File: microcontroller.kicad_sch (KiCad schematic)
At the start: 23 parts, among them J11 VOX_IN, J12 VOX_TRX, J6 I2C, J7 SW1_CON, J8 I2C, SW1 SW_Push, U3 ESP32-DEVKIT

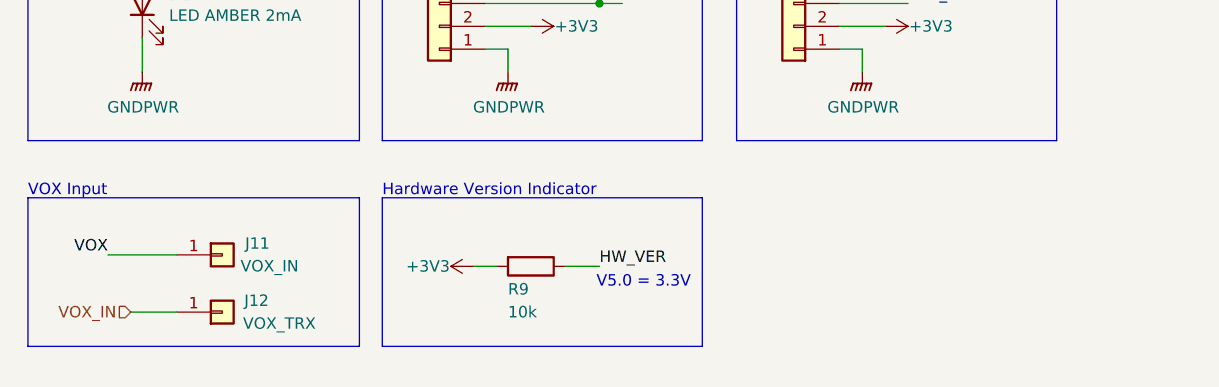
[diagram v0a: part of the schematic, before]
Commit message: am: Modified HW indication voltage
* Added R10 for voltage divider (v6.x == 1.65V)
* Replaced all R footprints with current ones from KiCad lib
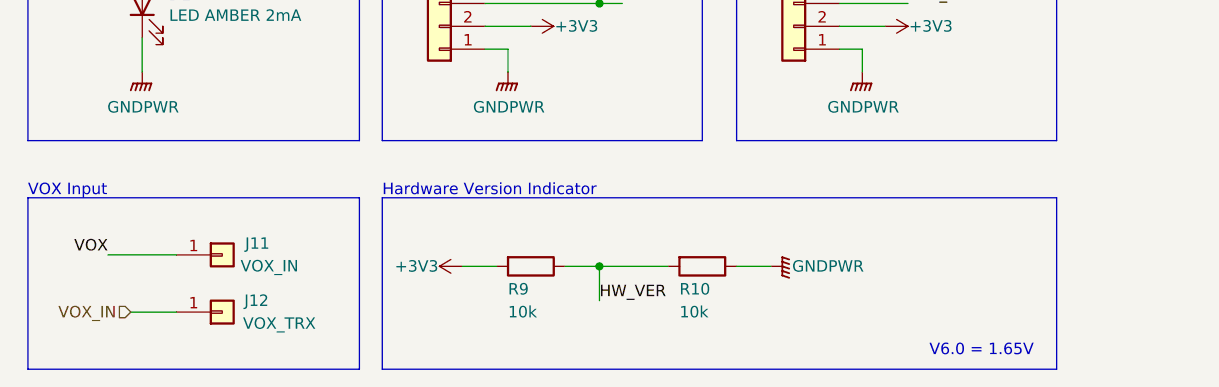
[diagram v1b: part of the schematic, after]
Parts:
- added R10: 10k, Resistor_SMD:R_0805_2012Metric_Pad1.20x1.40mm_HandSolder, symbol Device:R
- R2, R3, R4, R5, R6, R7, R9: footprint Resistor_SMD:R_0805_2012Metric_Pad1.15x1.40mm_HandSolder -> Resistor_SMD:R_0805_2012Metric_Pad1.20x1.40mm_HandSolder
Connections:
- net GNDPWR: now also R10.1
- net HW_VER: now also R10.2
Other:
- note added: "V6.0 = 1.65V"
- note removed: "V5.0 = 3.3V"
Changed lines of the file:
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@@
   (junction (at 30.48 72.39) (diameter 0) (color 0 0 0 0)
+  )
+  (junction (at 81.28 152.4) (diameter 0) (color 0 0 0 0)
   )
   (junction (at 24.13 72.39) (diameter 0) (color 0 0 0 0)
@@
     (stroke (width 0) (type default) (color 0 0 0 0))
   )
-  (polyline (pts (xy 54.61 144.78) (xy 54.61 161.29))
+  (polyline (pts (xy 54.61 144.78) (xy 54.61 163.83))
     (stroke (width 0) (type default) (color 0 0 0 0))
   )
@@
     (stroke (width 0) (type default) (color 0 0 0 0))
   )
-  (polyline (pts (xy 57.15 161.29) (xy 92.71 161.29))
+  (polyline (pts (xy 57.15 163.83) (xy 132.08 163.83))
     (stroke (width 0) (type default) (color 0 0 0 0))
   )
@@
     (stroke (width 0) (type default) (color 0 0 0 0))
   )
-  (polyline (pts (xy 92.71 144.78) (xy 57.15 144.78))
+  (polyline (pts (xy 132.08 144.78) (xy 57.15 144.78))
     (stroke (width 0) (type default) (color 0 0 0 0))
   )
@@
     (stroke (width 0) (type default) (color 0 0 0 0))
   )
-  (polyline (pts (xy 57.15 144.78) (xy 57.15 161.29))
+  (polyline (pts (xy 57.15 144.78) (xy 57.15 163.83))
     (stroke (width 0) (type default) (color 0 0 0 0))
   )
@@
     (stroke (width 0) (type default) (color 0 0 0 0))
   )
-  (wire (pts (xy 67.31 152.4) (xy 69.85 152.4))
-    (stroke (width 0) (type default) (color 0 0 0 0))
-  )
   (wire (pts (xy 81.28 116.84) (xy 81.28 123.19))
     (stroke (width 0) (type default) (color 0 0 0 0))
@@
     (stroke (width 0) (type default) (color 0 0 0 0))
   )
-  (polyline (pts (xy 17.78 144.78) (xy 17.78 161.29))
+  (polyline (pts (xy 17.78 144.78) (xy 17.78 163.83))
     (stroke (width 0) (type default) (color 0 0 0 0))
   )
@@
     (stroke (width 0) (type default) (color 0 0 0 0))
   )
-  (polyline (pts (xy 92.71 144.78) (xy 92.71 161.29))
+  (polyline (pts (xy 132.08 144.78) (xy 132.08 163.83))
     (stroke (width 0) (type default) (color 0 0 0 0))
   )
@@
     (stroke (width 0) (type default) (color 0 0 0 0))
   )
+  (wire (pts (xy 81.28 152.4) (xy 81.28 156.21))
+    (stroke (width 0) (type default) (color 0 0 0 0))
+  )
   (wire (pts (xy 171.45 58.42) (xy 175.26 58.42))
     (stroke (width 0) (type default) (color 0 0 0 0))
@@
     (stroke (width 0) (type default) (color 0 0 0 0))
   )
-  (polyline (pts (xy 54.61 161.29) (xy 17.78 161.29))
+  (polyline (pts (xy 54.61 163.83) (xy 17.78 163.83))
     (stroke (width 0) (type default) (color 0 0 0 0))
   )
@@
     (stroke (width 0) (type default) (color 0 0 0 0))
   )
+  (wire (pts (xy 96.52 152.4) (xy 100.33 152.4))
+    (stroke (width 0) (type default) (color 0 0 0 0))
+  )
   (wire (pts (xy 25.4 26.67) (xy 31.75 26.67))
     (stroke (width 0) (type default) (color 0 0 0 0))
@@
     (stroke (width 0) (type default) (color 0 0 0 0))
   )
+  (wire (pts (xy 81.28 152.4) (xy 88.9 152.4))
+    (stroke (width 0) (type default) (color 0 0 0 0))
+  )
   (wire (pts (xy 62.23 69.85) (xy 62.23 73.66))
     (stroke (width 0) (type default) (color 0 0 0 0))
   )
   (polyline (pts (xy 17.78 97.79) (xy 17.78 138.43))
+    (stroke (width 0) (type default) (color 0 0 0 0))
+  )
+  (wire (pts (xy 66.04 152.4) (xy 69.85 152.4))
     (stroke (width 0) (type default) (color 0 0 0 0))
   )
@@
     (effects (font (size 1.27 1.27)) (justify left bottom))
   )
-  (text "V5.0 = 3.3V" (at 91.44 154.94 180)
+  (text "V6.0 = 1.65V" (at 129.54 162.56 180)
     (effects (font (size 1.27 1.27)) (justify right bottom))
   )
@@
     (effects (font (size 1.27 1.27)) (justify right bottom))
   )
-  (label "HW_VER" (at 81.28 152.4 0)
+  (label "HW_VER" (at 81.28 156.21 0)
     (effects (font (size 1.27 1.27)) (justify left bottom))
   )
@@
       (effects (font (size 1.27 1.27)) (justify left))
     )
-    (property "Footprint" "Resistor_SMD:R_0805_2012Metric_Pad1.15x1.40mm_HandSolder" (id 2) (at 28.702 113.03 90)
+    (property "Footprint" "Resistor_SMD:R_0805_2012Metric_Pad1.20x1.40mm_HandSolder" (id 2) (at 28.702 113.03 90)
       (effects (font (size 1.27 1.27)) hide)
     )
@@
       (effects (font (size 1.27 1.27)) (justify left))
     )
-    (property "Footprint" "Resistor_SMD:R_0805_2012Metric_Pad1.15x1.40mm_HandSolder" (id 2) (at 60.452 66.04 90)
+    (property "Footprint" "Resistor_SMD:R_0805_2012Metric_Pad1.20x1.40mm_HandSolder" (id 2) (at 60.452 66.04 90)
       (effects (font (size 1.27 1.27)) hide)
     )
@@
       (effects (font (size 1.27 1.27)) (justify left))
     )
-    (property "Footprint" "Resistor_SMD:R_0805_2012Metric_Pad1.15x1.40mm_HandSolder" (id 2) (at 69.342 66.04 90)
+    (property "Footprint" "Resistor_SMD:R_0805_2012Metric_Pad1.20x1.40mm_HandSolder" (id 2) (at 69.342 66.04 90)
       (effects (font (size 1.27 1.27)) hide)
     )
@@
       (effects (font (size 1.27 1.27)) (justify left))
     )
-    (property "Footprint" "Resistor_SMD:R_0805_2012Metric_Pad1.15x1.40mm_HandSolder" (id 2) (at 71.882 113.03 90)
+    (property "Footprint" "Resistor_SMD:R_0805_2012Metric_Pad1.20x1.40mm_HandSolder" (id 2) (at 71.882 113.03 90)
       (effects (font (size 1.27 1.27)) hide)
     )
@@
       (effects (font (size 1.27 1.27)) (justify left))
     )
-    (property "Footprint" "Resistor_SMD:R_0805_2012Metric_Pad1.15x1.40mm_HandSolder" (id 2) (at 79.502 113.03 90)
+    (property "Footprint" "Resistor_SMD:R_0805_2012Metric_Pad1.20x1.40mm_HandSolder" (id 2) (at 79.502 113.03 90)
       (effects (font (size 1.27 1.27)) hide)
     )
@@
       (effects (font (size 1.27 1.27)) (justify left))
     )
-    (property "Footprint" "Resistor_SMD:R_0805_2012Metric_Pad1.15x1.40mm_HandSolder" (id 2) (at 28.702 66.04 90)
+    (property "Footprint" "Resistor_SMD:R_0805_2012Metric_Pad1.20x1.40mm_HandSolder" (id 2) (at 28.702 66.04 90)
       (effects (font (size 1.27 1.27)) hide)
     )
@@
       (effects (font (size 1.27 1.27)) (justify left))
     )
-    (property "Footprint" "Resistor_SMD:R_0805_2012Metric_Pad1.15x1.40mm_HandSolder" (id 2) (at 73.66 150.622 90)
+    (property "Footprint" "Resistor_SMD:R_0805_2012Metric_Pad1.20x1.40mm_HandSolder" (id 2) (at 73.66 150.622 90)
       (effects (font (size 1.27 1.27)) hide)
     )
@@
     (pin "1")
   )
-  (symbol (lib_id "power:+3V3") (at 67.31 152.4 90) (unit 1)
-    (in_bom yes) (on_board yes)
-    (property "Reference" "#PWR045" (id 0) (at 71.12 152.4 0)
-      (effects (font (size 1.27 1.27)) hide)
-    )
-    (property "Value" "+3V3" (id 1) (at 62.23 152.4 90))
-    (property "Footprint" "" (id 2) (at 67.31 152.4 0)
-      (effects (font (size 1.27 1.27)) hide)
-    )
-    (property "Datasheet" "" (id 3) (at 67.31 152.4 0)
+  (symbol (lib_id "power:+3V3") (at 66.04 152.4 90) (unit 1)
+    (in_bom yes) (on_board yes)
+    (property "Reference" "#PWR045" (id 0) (at 69.85 152.4 0)
+      (effects (font (size 1.27 1.27)) hide)
+    )
+    (property "Value" "+3V3" (id 1) (at 60.96 152.4 90))
+    (property "Footprint" "" (id 2) (at 66.04 152.4 0)
+      (effects (font (size 1.27 1.27)) hide)
+    )
+    (property "Datasheet" "" (id 3) (at 66.04 152.4 0)
       (effects (font (size 1.27 1.27)) hide)
     )
@@
       (effects (font (size 1.27 1.27)) hide)
     )
+    (pin "1")
+  )
+  (symbol (lib_id "Device:R") (at 92.71 152.4 270) (unit 1)
+    (in_bom yes) (on_board yes)
+    (property "Reference" "R10" (id 0) (at 90.17 154.94 90)
+      (effects (font (size 1.27 1.27)) (justify left))
+    )
+    (property "Value" "10k" (id 1) (at 90.17 157.48 90)
+      (effects (font (size 1.27 1.27)) (justify left))
+    )
+    (property "Footprint" "Resistor_SMD:R_0805_2012Metric_Pad1.20x1.40mm_HandSolder" (id 2) (at 92.71 150.622 90)
+      (effects (font (size 1.27 1.27)) hide)
+    )
+    (property "Datasheet" "~" (id 3) (at 92.71 152.4 0)
+      (effects (font (size 1.27 1.27)) hide)
+    )
+    (property "Mouser Best.Nr." "603-RC0805FR-0710KL" (id 4) (at 3.81 -69.85 0)
+      (effects (font (size 1.27 1.27)) hide)
+    )
+    (property "PartNrDigikey" "311-10.0KCRCT-ND" (id 5) (at 92.71 152.4 0)
+      (effects (font (size 1.27 1.27)) hide)
+    )
+    (pin "1")
+    (pin "2")
+  )
+  (symbol (lib_id "power:GNDPWR") (at 100.33 152.4 90) (unit 1)
+    (in_bom yes) (on_board yes)
+    (property "Reference" "#PWR03" (id 0) (at 105.41 152.4 0)
+      (effects (font (size 1.27 1.27)) hide)
+    )
+    (property "Value" "GNDPWR" (id 1) (at 106.68 152.4 90))
+    (property "Footprint" "" (id 2) (at 101.6 152.4 0)
+      (effects (font (size 1.27 1.27)) hide)
+    )
+    (property "Datasheet" "" (id 3) (at 101.6 152.4 0)
+      (effects (font (size 1.27 1.27)) hide)
+    )

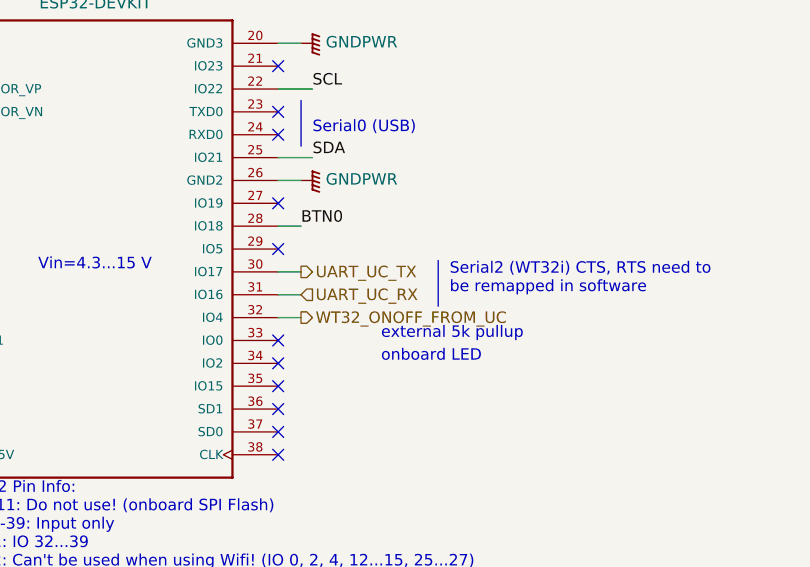
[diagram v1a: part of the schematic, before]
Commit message: am: Connected FMB100 RST pin to ESP
* Connected FMB100 RST pin to ESP in schematic and PCB
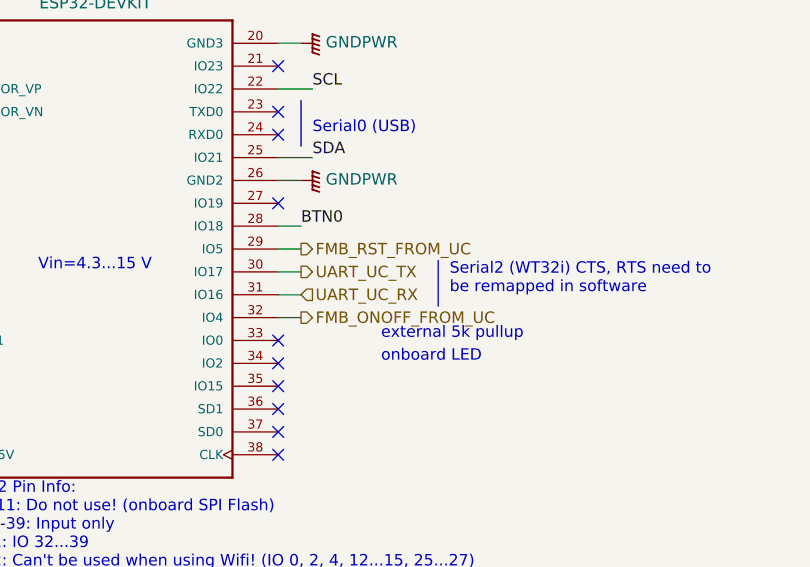
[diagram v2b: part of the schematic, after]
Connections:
- net FMB_RST_FROM_UC: now reaches U3.29 (IO5)
- net WT32_ONOFF_FROM_UC renamed FMB_ONOFF_FROM_UC
- no-connect marks 18 -> 17
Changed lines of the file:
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@@
   (no_connect (at 215.9 71.12))
   (no_connect (at 215.9 73.66))
-  (no_connect (at 215.9 55.88))
   (no_connect (at 215.9 35.56))
   (no_connect (at 215.9 78.74))
@@
     (stroke (width 0) (type default) (color 0 0 0 0))
   )
+  (wire (pts (xy 215.9 55.88) (xy 218.44 55.88))
+    (stroke (width 0) (type default) (color 0 0 0 0))
+  )
   (wire (pts (xy 60.96 26.67) (xy 60.96 27.94))
     (stroke (width 0) (type default) (color 0 0 0 0))
@@
     (effects (font (size 1.27 1.27)) (justify left bottom))
   )
-  (hierarchical_label "WT32_ONOFF_FROM_UC" (shape output) (at 218.44 63.5 0)
+  (hierarchical_label "FMB_ONOFF_FROM_UC" (shape output) (at 218.44 63.5 0)
     (effects (font (size 1.27 1.27)) (justify left))
   )
@@
     (effects (font (size 1.27 1.27)) (justify right))
   )
+  (hierarchical_label "FMB_RST_FROM_UC" (shape output) (at 218.44 55.88 0)
+    (effects (font (size 1.27 1.27)) (justify left))
+  )
   (hierarchical_label "PTT_OUT" (shape output) (at 172.72 50.8 180)
